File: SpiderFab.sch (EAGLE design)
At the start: 47 parts, among them IC1 SN754410, J14 5.5x2.1mm Barrel, U1 ATMEGA328, U3 MCP73831, X1 USBSMD, Y1 16MHz

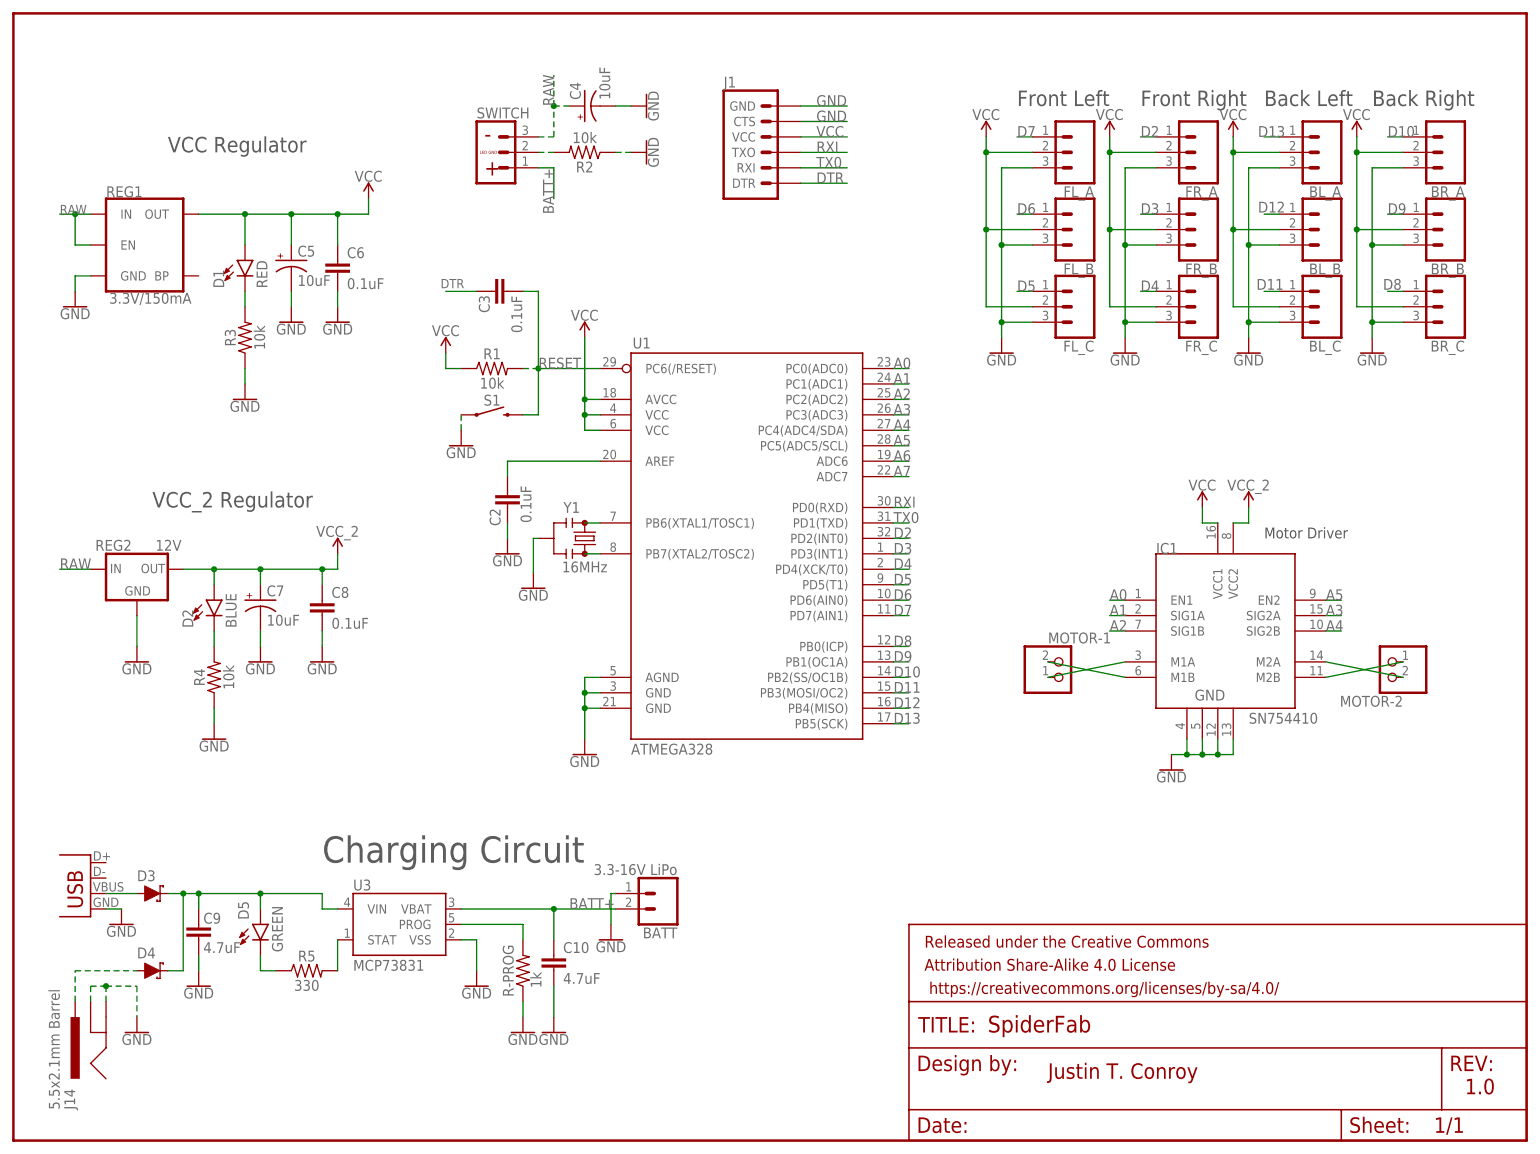
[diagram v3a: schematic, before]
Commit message: Swap some components for a different package.
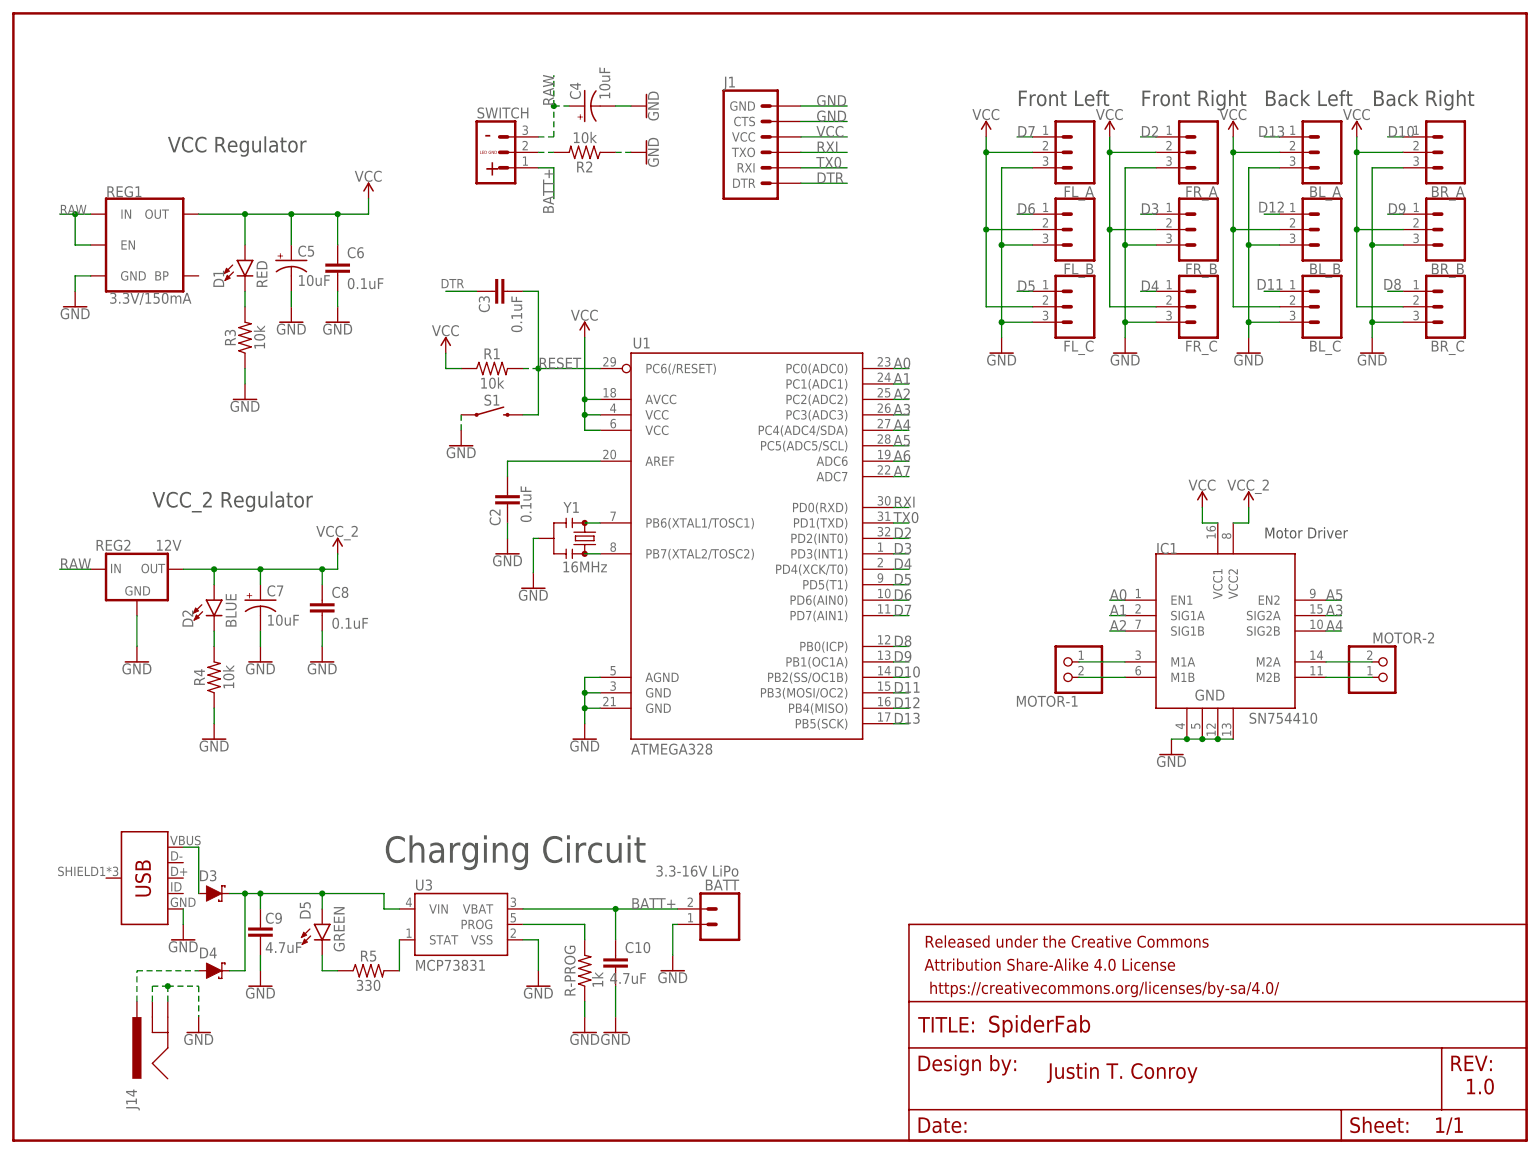
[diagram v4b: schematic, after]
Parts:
- J14: value 5.5x2.1mm Barrel -> POWER_JACK; device SparkFun-Connectors:POWER_JACKSMD -> SparkFun-Connectors:POWER_JACK
- X1: value USBSMD -> AMP FCI 10103594-0001LF; device SparkFun-Connectors:USBSMD -> SparkFun-Connectors:USB_MICRO-B_FEMALE-SMT
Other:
- moved on the sheet: BATT, C10, C9, D3, D4, D5, J14, MOTOR-1, MOTOR-2, R-PROG, R5, U3
